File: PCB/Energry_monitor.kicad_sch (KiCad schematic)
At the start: 0 parts

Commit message: feat(MCU): added MCU sheet
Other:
- added sheet MCU (MCU.kicad_sch)
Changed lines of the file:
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@@
 	(generator_version "9.0")
 	(paper "A4")
+	(sheet
+		(at 120.65 95.25)
+		(size 12.7 12.7)
+		(exclude_from_sim no)
+		(in_bom yes)
+		(on_board yes)
+		(dnp no)
+		(fields_autoplaced yes)
+		(stroke
+			(width 0.1524)
+			(type solid)
+		)
+		(fill
+			(color 0 0 0 0.0000)
+		)
+		(property "Sheetname" "MCU"
+			(at 120.65 94.5384 0)
+			(effects
+				(font
+					(size 1.27 1.27)
+				)
+				(justify left bottom)
+			)
+		)
+		(property "Sheetfile" "MCU.kicad_sch"
+			(at 120.65 108.5346 0)
+			(effects
+				(font
+					(size 1.27 1.27)
+				)
+				(justify left top)
+			)
+		)
+		(instances
+			(project "Energry_monitor"
+				(path "/b3a00096-e201-45d6-8313-ccf00a75c96f"
+					(page "2")
+				)
+			)
+		)
+	)
 	(sheet_instances
 		(path "/"

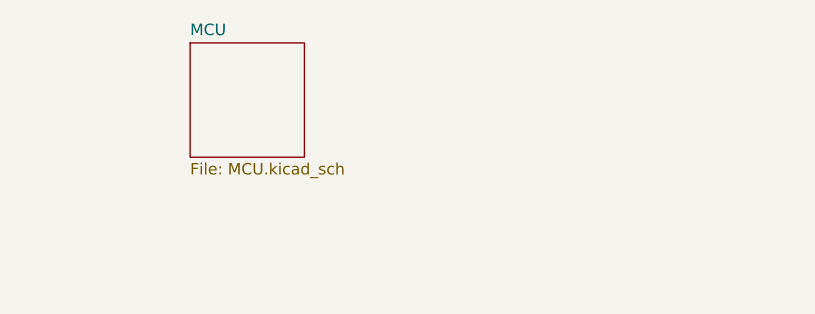
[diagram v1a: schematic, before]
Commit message: feat(POWER): introduced a dual ldo power tree with a 230-5v supply
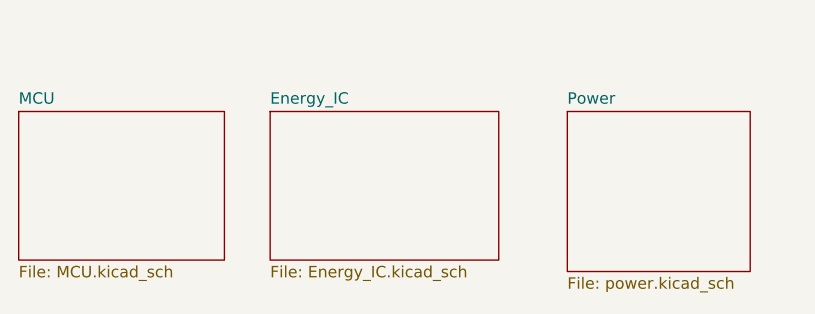
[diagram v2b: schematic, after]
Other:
- added sheet Energy_IC (Energy_IC.kicad_sch)
- added sheet Power (power.kicad_sch)
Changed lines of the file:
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@@
 	(paper "A4")
 	(sheet
-		(at 120.65 95.25)
-		(size 12.7 12.7)
+		(at 162.56 102.87)
+		(size 20.32 17.78)
+		(exclude_from_sim no)
+		(in_bom yes)
+		(on_board yes)
+		(dnp no)
+		(fields_autoplaced yes)
+		(stroke
+			(width 0.1524)
+			(type solid)
+		)
+		(fill
+			(color 0 0 0 0.0000)
+		)
+		(property "Sheetname" "Power"
+			(at 162.56 102.1584 0)
+			(effects
+				(font
+					(size 1.27 1.27)
+				)
+				(justify left bottom)
+			)
+		)
+		(property "Sheetfile" "power.kicad_sch"
+			(at 162.56 121.2346 0)
+			(effects
+				(font
+					(size 1.27 1.27)
+				)
+				(justify left top)
+			)
+		)
+		(instances
+			(project "Energry_monitor"
+				(path "/b3a00096-e201-45d6-8313-ccf00a75c96f"
+					(page "3")
+				)
+			)
+		)
+	)
+	(sheet
+		(at 129.54 102.87)
+		(size 25.4 16.51)
+		(exclude_from_sim no)
+		(in_bom yes)
+		(on_board yes)
+		(dnp no)
+		(fields_autoplaced yes)
+		(stroke
+			(width 0.1524)
+			(type solid)
+		)
+		(fill
+			(color 0 0 0 0.0000)
+		)
+		(property "Sheetname" "Energy_IC"
+			(at 129.54 102.1584 0)
+			(effects
+				(font
+					(size 1.27 1.27)
+				)
+				(justify left bottom)
+			)
+		)
+		(property "Sheetfile" "Energy_IC.kicad_sch"
+			(at 129.54 119.9646 0)
+			(effects
+				(font
+					(size 1.27 1.27)
+				)
+				(justify left top)
+			)
+		)
+		(instances
+			(project "Energry_monitor"
+				(path "/b3a00096-e201-45d6-8313-ccf00a75c96f"
+					(page "4")
+				)
+			)
+		)
+	)
+	(sheet
+		(at 101.6 102.87)
+		(size 22.86 16.51)
 		(exclude_from_sim no)
 		(in_bom yes)
@@
 		)
 		(property "Sheetname" "MCU"
-			(at 120.65 94.5384 0)
+			(at 101.6 102.1584 0)
 			(effects
 				(font
@@
 		)
 		(property "Sheetfile" "MCU.kicad_sch"
-			(at 120.65 108.5346 0)
+			(at 101.6 119.9646 0)
 			(effects
 				(font
